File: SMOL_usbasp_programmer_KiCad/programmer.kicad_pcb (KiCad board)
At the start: 2 copper layers, 17.8 x 41.3 mm, 9 parts, among them CON1 AVR-TPI-6, CON2 AVR-ISP-10, J2 Conn_01x05

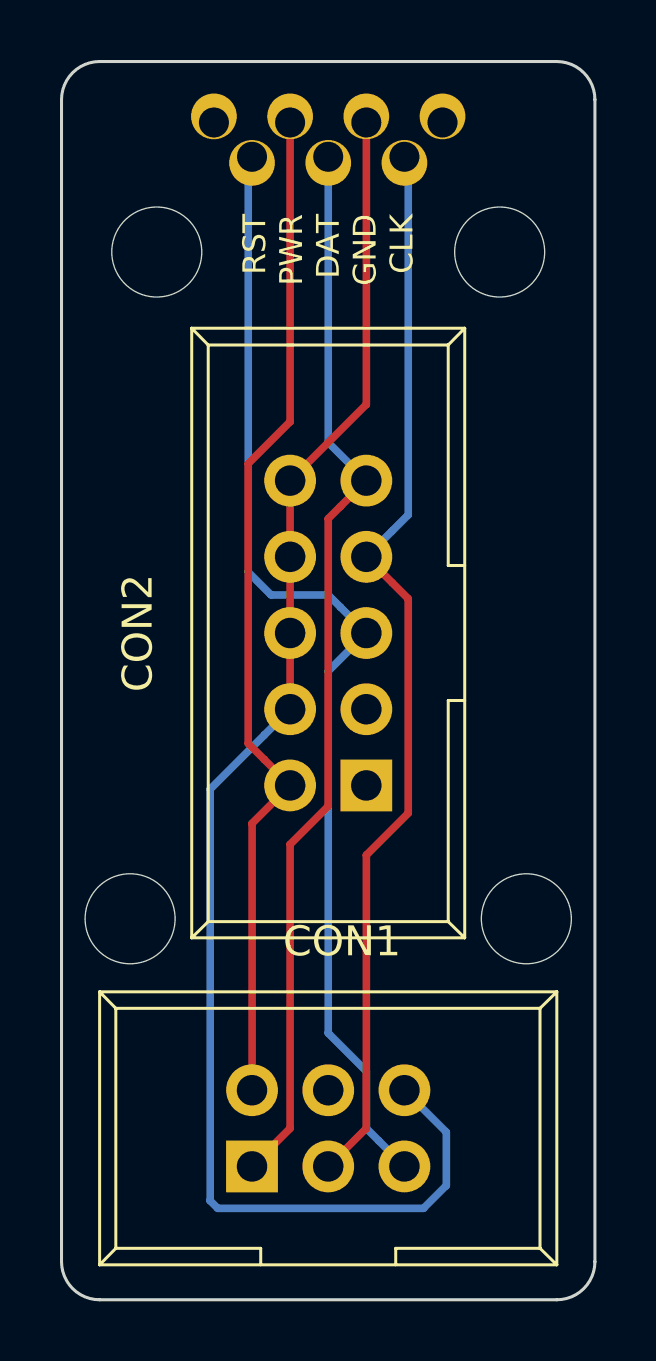
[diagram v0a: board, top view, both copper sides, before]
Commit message: FINALLY fixed the anchor points for mounting holes on SMOL and programmers. Added OSHW logo to library, just in case....
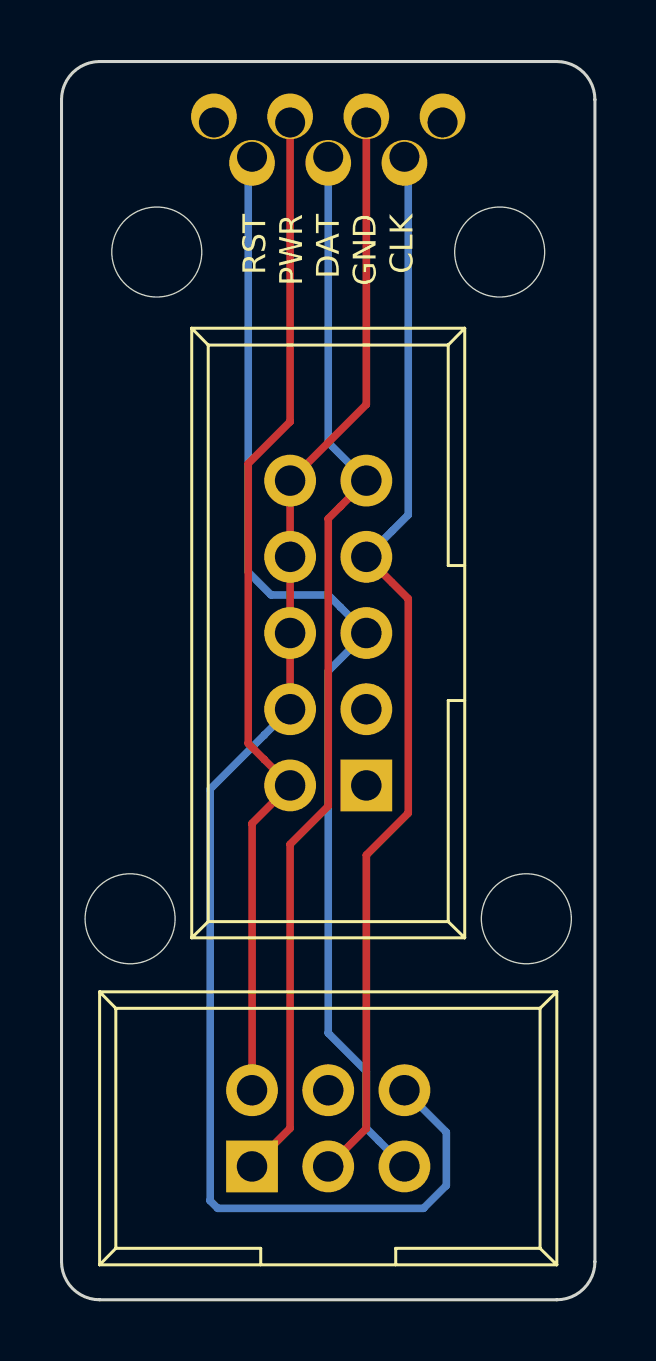
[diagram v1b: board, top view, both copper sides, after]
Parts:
- moved HOLE6 1.92 mm to (31.8, 14.1)
- moved HOLE5 1.92 mm to (24.1, 14.1)
- renumbered REF** to HOLE1, REF** to HOLE2, REF** to HOLE3, REF** to HOLE4, REF** to HOLE5, REF** to HOLE6
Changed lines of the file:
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@@
     (mod_text_size 1 1)
     (mod_text_width 0.15)
-    (pad_size 2.999999 2.999999)
-    (pad_drill 2.999999)
+    (pad_size 1.524 1.524)
+    (pad_drill 1)
     (pad_to_mask_clearance 0.0508)
     (solder_mask_min_width 0.25)
@@
     (tags "mounting hole 3.2mm no annular m3")
     (attr virtual)
-    (fp_text reference REF** (at 0 -4.2) (layer F.SilkS) hide
+    (fp_text reference HOLE4 (at 0 -4.2) (layer F.SilkS) hide
       (effects (font (size 1 1) (thickness 0.15)))
     )
@@
     (descr "6 pins through hole IDC header")
     (tags "IDC header socket VASCH AVR ISP")
-    (fp_text reference CON1 (at 3 -7.5) (layer F.SilkS)
+    (fp_text reference CON1 (at 3 -7.5) (layer F.SilkS) hide
       (effects (font (size 1 1) (thickness 0.15)))
     )
@@
     (descr "10 pins through hole IDC header")
     (tags "IDC header socket VASCH")
-    (fp_text reference CON2 (at 5.08 -7.62 90) (layer F.SilkS)
+    (fp_text reference CON2 (at 5.08 -7.62 90) (layer F.SilkS) hide
       (effects (font (size 1 1) (thickness 0.15)))
     )
@@
   )
   (module Wire_Pads:SolderWirePad_single_1mmDrill (layer F.Cu)
-    (at 29.845 14.351 90)
-    (fp_text reference REF** (at 0 -3.81 90) (layer F.SilkS) hide
+    (at 31.75 14.097 90)
+    (fp_text reference HOLE6 (at 0 -3.81 90) (layer F.SilkS) hide
       (effects (font (size 1 1) (thickness 0.15)))
     )
@@
       (effects (font (size 1 1) (thickness 0.15)))
     )
-    (pad 1 thru_hole oval (at 0.254 1.905 90) (size 1.524 1.524) (drill 1 (offset 0.2032 0)) (layers *.Cu *.Mask))
+    (pad 1 thru_hole oval (at 0 0 90) (size 1.524 1.524) (drill 1 (offset 0.2032 0)) (layers *.Cu *.Mask))
   )
   (module Mounting_Holes:MountingHole_3.2mm_M3 (layer F.Cu)
@@
     (tags "mounting hole 3.2mm no annular m3")
     (attr virtual)
-    (fp_text reference REF** (at 0 -4.2) (layer F.SilkS) hide
+    (fp_text reference HOLE2 (at 0 -4.2) (layer F.SilkS) hide
       (effects (font (size 1 1) (thickness 0.15)))
     )
@@
     (tags "mounting hole 3.2mm no annular m3")
     (attr virtual)
-    (fp_text reference REF** (at 0 -4.2) (layer F.SilkS) hide
+    (fp_text reference HOLE3 (at 0 -4.2) (layer F.SilkS) hide
       (effects (font (size 1 1) (thickness 0.15)))
     )
@@
     (tags "mounting hole 3.2mm no annular m3")
     (attr virtual)
-    (fp_text reference REF** (at 0 -4.2) (layer F.SilkS) hide
+    (fp_text reference HOLE1 (at 0 -4.2) (layer F.SilkS) hide
       (effects (font (size 1 1) (thickness 0.15)))
     )
@@
   )
   (module Wire_Pads:SolderWirePad_single_1mmDrill (layer F.Cu)
-    (at 22.225 14.351 90)
-    (fp_text reference REF** (at 0 -3.81 90) (layer F.SilkS) hide
+    (at 24.13 14.097 90)
+    (fp_text reference HOLE5 (at 0 -3.81 90) (layer F.SilkS) hide
       (effects (font (size 1 1) (thickness 0.15)))
     )
@@
       (effects (font (size 1 1) (thickness 0.15)))
     )
-    (pad 1 thru_hole oval (at 0.254 1.905 90) (size 1.524 1.524) (drill 1 (offset 0.2032 0)) (layers *.Cu *.Mask))
+    (pad 1 thru_hole oval (at 0 0 90) (size 1.524 1.524) (drill 1 (offset 0.2032 0)) (layers *.Cu *.Mask))
   )
   (gr_text CLK (at 31.75 28.575) (layer B.SilkS)

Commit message: Updated the USBasp programmer; updated programmer silkscreens
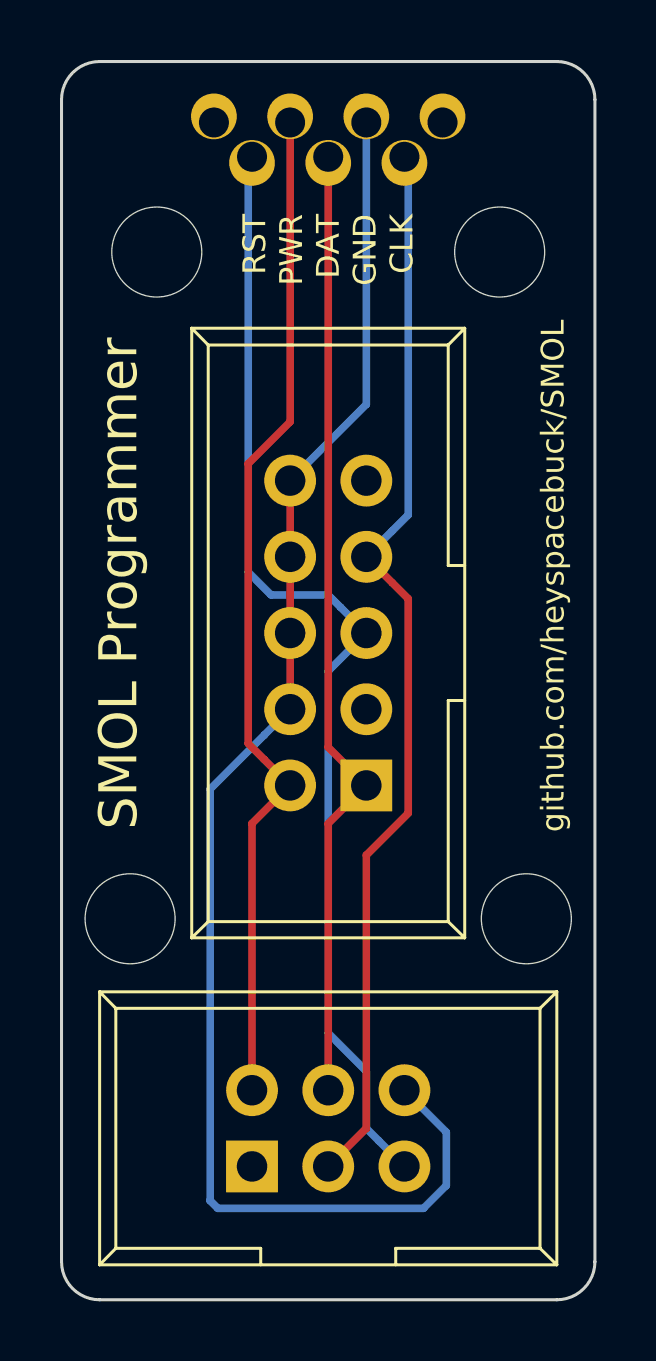
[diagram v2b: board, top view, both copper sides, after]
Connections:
- CON1 pad 1: /att_data -> (no net)
- CON1 pad 4: Net-(CON1-Pad4) -> /att_data
- CON2 pad 1: Net-(CON2-Pad1) -> /att_data
- CON2 pad 9: /att_data -> (no net)
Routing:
- net /att_data: track 35.8 -> 32.2 mm
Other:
- board text added: "SMOL Programmer"
- board text added: "github.com/heyspacebuck/SMOL"
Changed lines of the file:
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@@
   (general
     (thickness 1.6)
-    (drawings 25)
-    (tracks 50)
+    (drawings 27)
+    (tracks 46)
     (zones 0)
     (modules 9)
-    (nets 9)
+    (nets 7)
   )
   (page USLetter)
@@
     (mod_text_size 1 1)
     (mod_text_width 0.15)
-    (pad_size 1.524 1.524)
-    (pad_drill 1)
+    (pad_size 1.7272 1.7272)
+    (pad_drill 1.016)
     (pad_to_mask_clearance 0.0508)
     (solder_mask_min_width 0.25)
@@
   (net 4 GNDREF)
   (net 5 /att_clk)
-  (net 6 "Net-(CON1-Pad4)")
-  (net 7 "Net-(CON2-Pad1)")
-  (net 8 "Net-(CON2-Pad3)")
+  (net 6 "Net-(CON2-Pad3)")
   (net_class Default "This is the default net class."
     (clearance 0.2032)
@@
     (add_net /pwr)
     (add_net GNDREF)
-    (add_net "Net-(CON1-Pad4)")
-    (add_net "Net-(CON2-Pad1)")
     (add_net "Net-(CON2-Pad3)")
   )
@@
       (effects (font (size 1 1) (thickness 0.12)))
     )
-    (pad 1 thru_hole rect (at 0 0) (size 1.7272 1.7272) (drill 1.016) (layers *.Cu *.Mask)
-      (net 3 /att_data))
+    (pad 1 thru_hole rect (at 0 0) (size 1.7272 1.7272) (drill 1.016) (layers *.Cu *.Mask))
     (pad 2 thru_hole oval (at 0 -2.54) (size 1.7272 1.7272) (drill 1.016) (layers *.Cu *.Mask)
       (net 1 /pwr))
@@
       (net 5 /att_clk))
     (pad 4 thru_hole oval (at 2.54 -2.54) (size 1.7272 1.7272) (drill 1.016) (layers *.Cu *.Mask)
-      (net 6 "Net-(CON1-Pad4)"))
+      (net 3 /att_data))
     (pad 5 thru_hole oval (at 5.08 0) (size 1.7272 1.7272) (drill 1.016) (layers *.Cu *.Mask)
       (net 2 /att_reset))
@@
     )
     (pad 1 thru_hole rect (at 0 0 90) (size 1.7272 1.7272) (drill 1.016) (layers *.Cu *.Mask)
-      (net 7 "Net-(CON2-Pad1)"))
+      (net 3 /att_data))
     (pad 2 thru_hole oval (at 0 -2.54 90) (size 1.7272 1.7272) (drill 1.016) (layers *.Cu *.Mask)
       (net 1 /pwr))
     (pad 3 thru_hole oval (at 2.54 0 90) (size 1.7272 1.7272) (drill 1.016) (layers *.Cu *.Mask)
-      (net 8 "Net-(CON2-Pad3)"))
+      (net 6 "Net-(CON2-Pad3)"))
     (pad 4 thru_hole oval (at 2.54 -2.54 90) (size 1.7272 1.7272) (drill 1.016) (layers *.Cu *.Mask)
       (net 4 GNDREF))
@@
     (pad 8 thru_hole oval (at 7.62 -2.54 90) (size 1.7272 1.7272) (drill 1.016) (layers *.Cu *.Mask)
       (net 4 GNDREF))
-    (pad 9 thru_hole oval (at 10.16 0 90) (size 1.7272 1.7272) (drill 1.016) (layers *.Cu *.Mask)
-      (net 3 /att_data))
+    (pad 9 thru_hole oval (at 10.16 0 90) (size 1.7272 1.7272) (drill 1.016) (layers *.Cu *.Mask))
     (pad 10 thru_hole oval (at 10.16 -2.54 90) (size 1.7272 1.7272) (drill 1.016) (layers *.Cu *.Mask)
       (net 4 GNDREF))
@@
     (pad 1 thru_hole oval (at 0 0 90) (size 1.524 1.524) (drill 1 (offset 0.2032 0)) (layers *.Cu *.Mask))
   )
+  (gr_text github.com/heyspacebuck/SMOL (at 35.433 29.21 90) (layer F.SilkS)
+    (effects (font (size 0.762 0.762) (thickness 0.1778)))
+  )
+  (gr_text "SMOL Programmer" (at 20.955 29.464 90) (layer F.SilkS)
+    (effects (font (size 1.27 1.27) (thickness 0.254)))
+  )
   (gr_text CLK (at 31.75 28.575) (layer B.SilkS)
     (effects (font (size 0.762 0.762) (thickness 0.15875)) (justify mirror))
   )
-  (gr_text MOSI (at 31.75 26.035) (layer B.SilkS)
+  (gr_text N/C (at 31.75 26.035) (layer B.SilkS)
     (effects (font (size 0.762 0.762) (thickness 0.15875)) (justify mirror))
   )
@@
     (effects (font (size 0.762 0.762) (thickness 0.15875)) (justify mirror))
   )
-  (gr_text N/C (at 31.75 36.195) (layer B.SilkS)
+  (gr_text MOSI (at 31.75 36.195) (layer B.SilkS)
     (effects (font (size 0.762 0.762) (thickness 0.15875)) (justify mirror))
   )
@@
     (effects (font (size 0.762 0.762) (thickness 0.15875)) (justify mirror))
   )
-  (gr_text N/C (at 27.94 44.45) (layer B.SilkS)
-    (effects (font (size 0.762 0.762) (thickness 0.15875)) (justify mirror))
-  )
-  (gr_text MOSI (at 24.765 50.8) (layer B.SilkS)
+  (gr_text MOSI (at 27.94 44.45) (layer B.SilkS)
+    (effects (font (size 0.762 0.762) (thickness 0.15875)) (justify mirror))
+  )
+  (gr_text N/C (at 24.765 50.8) (layer B.SilkS)
     (effects (font (size 0.762 0.762) (thickness 0.15875)) (justify mirror))
   )
@@
   (segment (start 25.4 15.24) (end 25.273 15.367) (width 0.254) (layer B.Cu) (net 2))
   (segment (start 25.273 15.367) (end 25.273 29.083) (width 0.254) (layer B.Cu) (net 2))
-  (segment (start 27.94 24.765) (end 29.21 26.035) (width 0.254) (layer B.Cu) (net 3))
-  (segment (start 27.94 15.24) (end 27.94 24.765) (width 0.254) (layer B.Cu) (net 3))
-  (segment (start 28.346401 26.898599) (end 29.21 26.035) (width 0.254) (layer F.Cu) (net 3))
-  (segment (start 27.94 27.305) (end 28.346401 26.898599) (width 0.254) (layer F.Cu) (net 3))
-  (segment (start 27.94 36.887913) (end 27.94 27.305) (width 0.254) (layer F.Cu) (net 3))
-  (segment (start 26.67 38.157913) (end 27.94 36.887913) (width 0.254) (layer F.Cu) (net 3))
-  (segment (start 25.4 48.895) (end 26.67 47.625) (width 0.254) (layer F.Cu) (net 3))
-  (segment (start 26.67 47.625) (end 26.67 38.157913) (width 0.254) (layer F.Cu) (net 3))
+  (segment (start 27.94 37.465) (end 29.21 36.195) (width 0.254) (layer F.Cu) (net 3))
+  (segment (start 27.94 46.355) (end 27.94 37.465) (width 0.254) (layer F.Cu) (net 3))
+  (segment (start 27.94 34.925) (end 27.94 15.24) (width 0.254) (layer F.Cu) (net 3))
+  (segment (start 29.21 36.195) (end 27.94 34.925) (width 0.254) (layer F.Cu) (net 3))
   (segment (start 26.67 33.655) (end 26.67 31.115) (width 0.254) (layer F.Cu) (net 4))
   (segment (start 26.67 31.115) (end 26.67 28.575) (width 0.254) (layer F.Cu) (net 4))
   (segment (start 26.67 28.575) (end 26.67 26.035) (width 0.254) (layer F.Cu) (net 4))
-  (segment (start 29.21 23.495) (end 29.21 14.097) (width 0.254) (layer F.Cu) (net 4))
-  (segment (start 26.67 26.035) (end 29.21 23.495) (width 0.254) (layer F.Cu) (net 4))
+  (segment (start 29.21 23.495) (end 29.21 14.097) (width 0.254) (layer B.Cu) (net 4))
+  (segment (start 26.67 26.035) (end 29.21 23.495) (width 0.254) (layer B.Cu) (net 4))
   (segment (start 24.003 36.322) (end 25.806401 34.518599) (width 0.254) (layer B.Cu) (net 4))
   (segment (start 31.877 47.752) (end 31.877 49.53) (width 0.254) (layer B.Cu) (net 4))
